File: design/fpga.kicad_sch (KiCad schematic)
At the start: 83 parts, among them J7 DEBUG_FPGA_GPIO, J8 DIGILENT_JTAG_HS2_01X06, SW1 RST, SW2 PROG, U13 XC7S15-FTGB196, U14 IS25LP064A-JKx

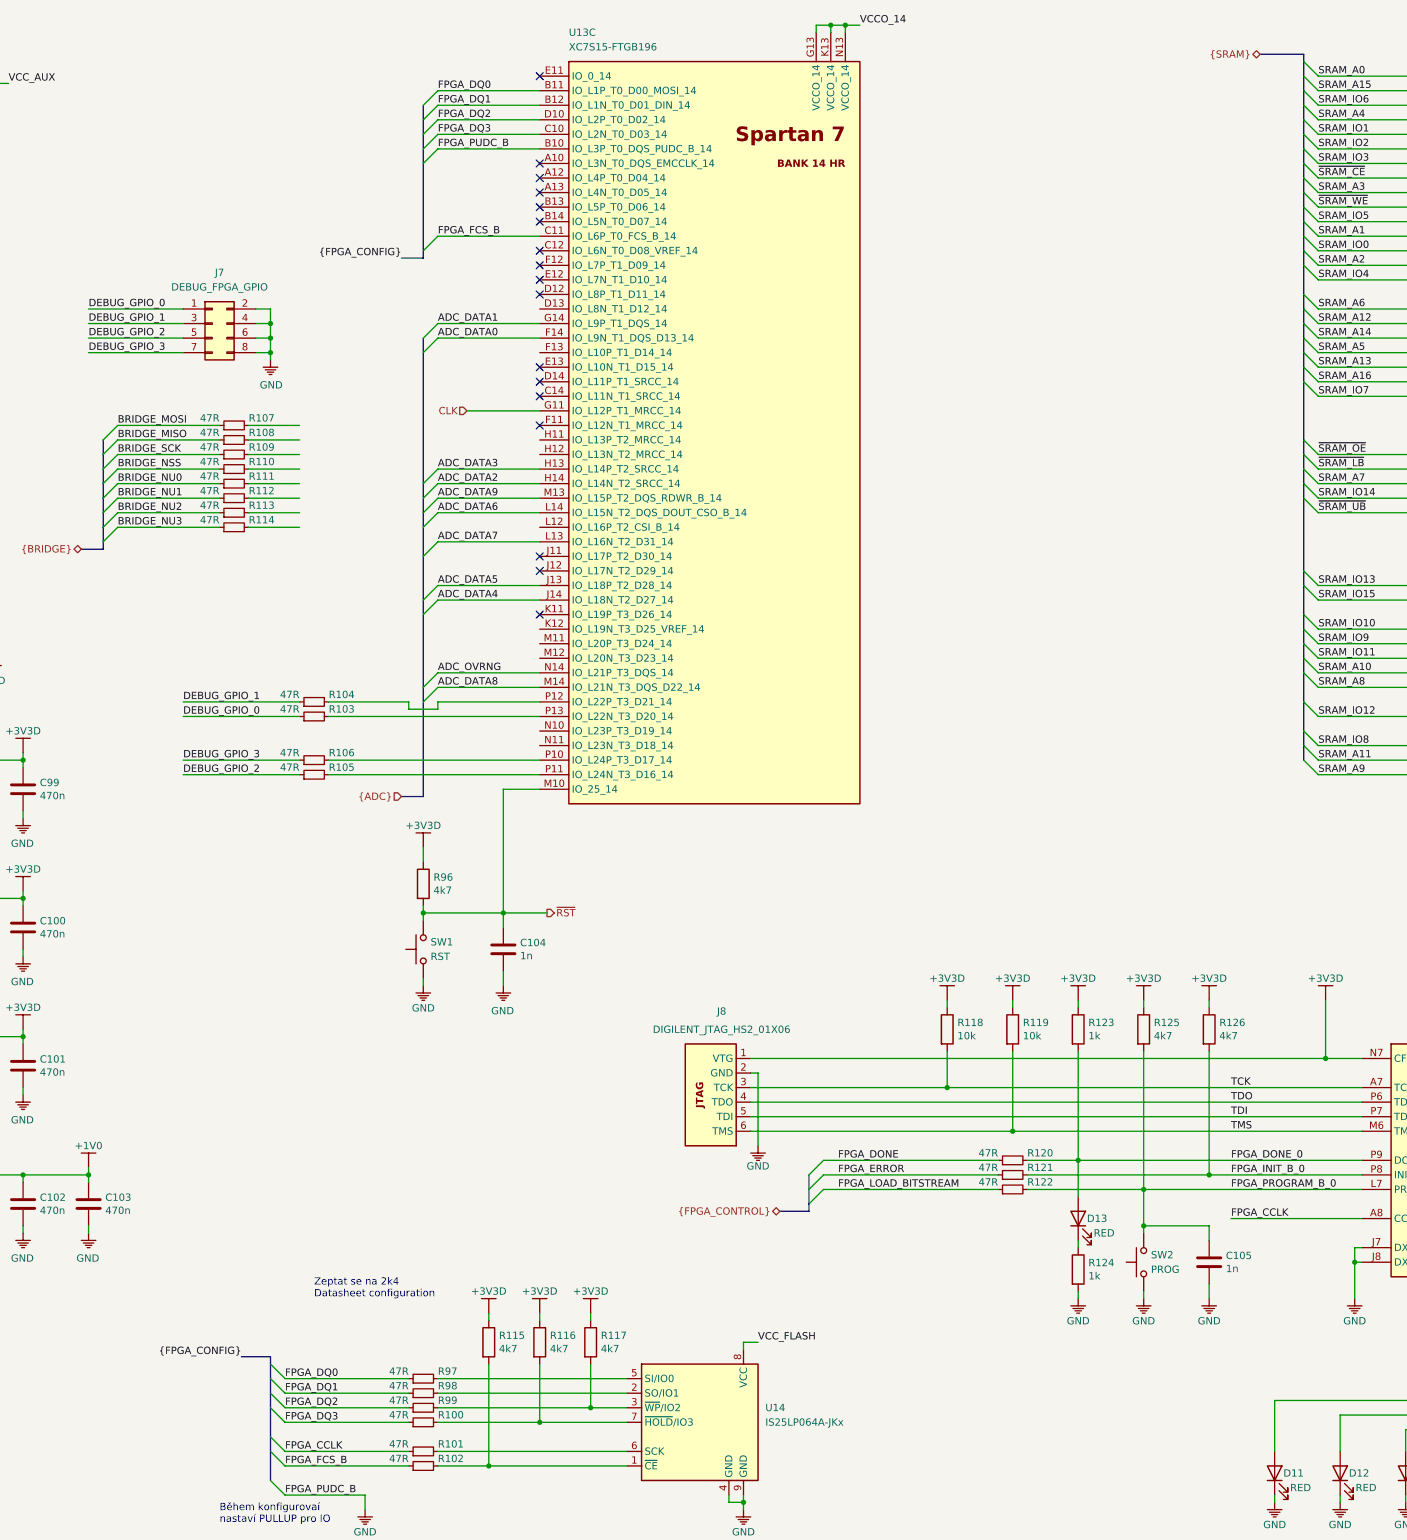
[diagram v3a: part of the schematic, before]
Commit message: Updated layout
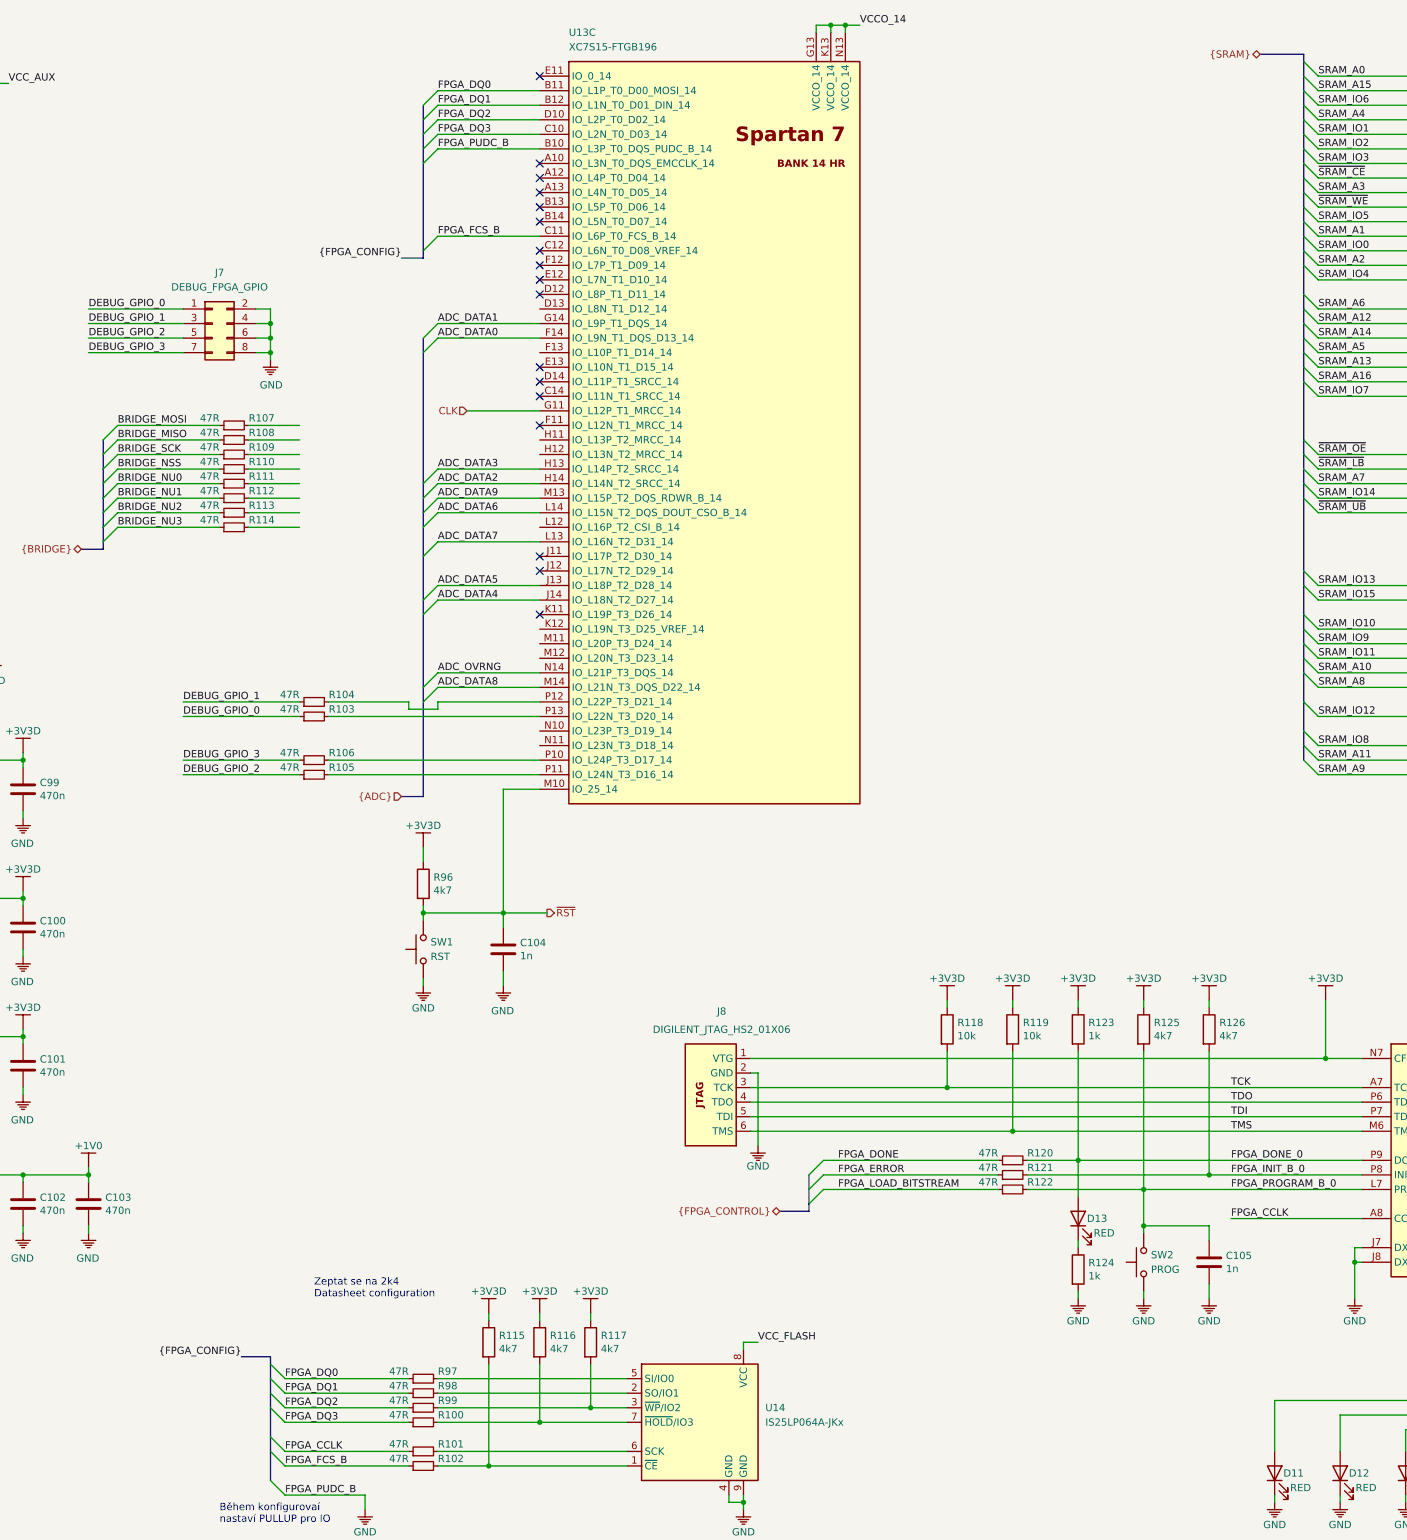
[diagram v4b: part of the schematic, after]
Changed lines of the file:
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@@
 (kicad_sch (version 20200512) (host eeschema "5.99.0-unknown-2cf82d9~101~ubuntu18.04.1")
-  (page 8 8)
+  (page 1 8)
   (paper "A3")
   (title_block
@@
     (company "Jan Vykydal")
   )
+  (bus_alias "FPGA_CONTROL" (members "FPGA_DONE" "FPGA_ERROR" "FPGA_LOAD_BITSTREAM"))
   (bus_alias "FPGA_CONFIG" (members "FPGA_DQ[0..3]" "FPGA_CCLK" "FPGA_FCS_B" "FPGA_PUDC_B"))
   (bus_alias "BRIDGE" (members "BRIDGE_MOSI" "BRIDGE_MISO" "BRIDGE_SCK" "BRIDGE_NSS" "BRIDGE_NU[0..3]"))
-  (bus_alias "FPGA_CONTROL" (members "FPGA_DONE" "FPGA_ERROR" "FPGA_LOAD_BITSTREAM"))
   (junction (at 26.67 26.67))
   (junction (at 26.67 29.21))
@@
   (junction (at 391.16 232.41))
   (junction (at 392.43 16.51))
+  (no_connect (at 185.42 63.5))
+  (no_connect (at 185.42 111.76))
+  (no_connect (at 185.42 25.4))
   (no_connect (at 185.42 58.42))
+  (no_connect (at 185.42 60.96))
   (no_connect (at 185.42 45.72))
-  (no_connect (at 185.42 48.26))
-  (no_connect (at 185.42 111.76))
-  (no_connect (at 185.42 109.22))
-  (no_connect (at 185.42 60.96))
-  (no_connect (at 185.42 63.5))
   (no_connect (at 185.42 55.88))
-  (no_connect (at 185.42 40.64))
-  (no_connect (at 185.42 119.38))
-  (no_connect (at 185.42 86.36))
-  (no_connect (at 185.42 78.74))
   (no_connect (at 185.42 76.2))
-  (no_connect (at 185.42 81.28))
-  (no_connect (at 185.42 25.4))
   (no_connect (at 185.42 50.8))
   (no_connect (at 185.42 43.18))
+  (no_connect (at 185.42 119.38))
+  (no_connect (at 185.42 109.22))
+  (no_connect (at 185.42 86.36))
+  (no_connect (at 185.42 40.64))
+  (no_connect (at 185.42 48.26))
+  (no_connect (at 185.42 78.74))
+  (no_connect (at 185.42 81.28))
   (bus_entry (at 109.22 88.9) (size 2.54 -2.54))
   (bus_entry (at 109.22 91.44) (size 2.54 -2.54))
@@
   (wire (pts (xy 392.43 16.51) (xy 394.97 16.51)))
   (bus (pts (xy 105.41 107.95) (xy 109.22 107.95)))
-  (bus (pts (xy 109.22 88.9) (xy 109.22 91.44)))
-  (bus (pts (xy 109.22 91.44) (xy 109.22 96.52)))
-  (bus (pts (xy 109.22 96.52) (xy 109.22 99.06)))
+  (bus (pts (xy 109.22 88.9) (xy 109.22 93.98)))
+  (bus (pts (xy 109.22 93.98) (xy 109.22 99.06)))
   (bus (pts (xy 109.22 99.06) (xy 109.22 104.14)))
   (bus (pts (xy 109.22 104.14) (xy 109.22 107.95)))
   (bus (pts (xy 133.35 248.92) (xy 138.43 248.92)))
   (bus (pts (xy 138.43 248.92) (xy 138.43 252.73)))
-  (bus (pts (xy 138.43 252.73) (xy 138.43 255.27)))
-  (bus (pts (xy 138.43 255.27) (xy 138.43 262.89)))
+  (bus (pts (xy 138.43 252.73) (xy 138.43 257.81)))
+  (bus (pts (xy 138.43 257.81) (xy 138.43 262.89)))
   (bus (pts (xy 138.43 262.89) (xy 138.43 270.51)))
   (bus (pts (xy 161.29 57.15) (xy 165.1 57.15)))
   (bus (pts (xy 161.29 151.13) (xy 165.1 151.13)))
   (bus (pts (xy 165.1 30.48) (xy 165.1 35.56)))
-  (bus (pts (xy 165.1 35.56) (xy 165.1 40.64)))
-  (bus (pts (xy 165.1 40.64) (xy 165.1 57.15)))
+  (bus (pts (xy 165.1 35.56) (xy 165.1 38.1)))
+  (bus (pts (xy 165.1 38.1) (xy 165.1 55.88)))
+  (bus (pts (xy 165.1 55.88) (xy 165.1 57.15)))
   (bus (pts (xy 165.1 71.12) (xy 165.1 96.52)))
   (bus (pts (xy 165.1 96.52) (xy 165.1 101.6)))
@@
   (bus (pts (xy 232.41 222.25) (xy 232.41 223.52)))
   (bus (pts (xy 318.77 21.59) (xy 311.15 21.59)))
-  (bus (pts (xy 318.77 21.59) (xy 318.77 22.86)))
-  (bus (pts (xy 318.77 22.86) (xy 318.77 27.94)))
-  (bus (pts (xy 318.77 27.94) (xy 318.77 33.02)))
+  (bus (pts (xy 318.77 21.59) (xy 318.77 25.4)))
+  (bus (pts (xy 318.77 25.4) (xy 318.77 30.48)))
+  (bus (pts (xy 318.77 30.48) (xy 318.77 33.02)))
   (bus (pts (xy 318.77 33.02) (xy 318.77 38.1)))
-  (bus (pts (xy 318.77 38.1) (xy 318.77 40.64)))
-  (bus (pts (xy 318.77 40.64) (xy 318.77 45.72)))
-  (bus (pts (xy 318.77 45.72) (xy 318.77 50.8)))
-  (bus (pts (xy 318.77 50.8) (xy 318.77 55.88)))
-  (bus (pts (xy 318.77 55.88) (xy 318.77 58.42)))
+  (bus (pts (xy 318.77 38.1) (xy 318.77 43.18)))
+  (bus (pts (xy 318.77 43.18) (xy 318.77 48.26)))
+  (bus (pts (xy 318.77 48.26) (xy 318.77 53.34)))
+  (bus (pts (xy 318.77 53.34) (xy 318.77 58.42)))
   (bus (pts (xy 318.77 58.42) (xy 318.77 66.04)))
   (bus (pts (xy 318.77 66.04) (xy 318.77 71.12)))
